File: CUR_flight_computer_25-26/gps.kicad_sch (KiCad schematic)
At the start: 4 parts, among them U1 SAM-M8Q

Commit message: Revert "edited gps"
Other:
- note removed: "Leave as 0 for now can be used for emi protection (R>20), ferrite beads, inductors but may affect signal timing"
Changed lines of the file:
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@@
 	(generator_version "9.0")
 	(paper "A4")
-	(text "Leave as 0 for now\ncan be used for emi protection\n(R>20), ferrite beads, inductors\nbut may affect signal timing"
-		(exclude_from_sim no)
-		(at 179.578 92.964 0)
-		(effects
-			(font
-				(size 1.27 1.27)
-			)
-		)
-	)
 	(text "Funky ass RX/TX switcher"
 		(exclude_from_sim no)

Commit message: added dubugging
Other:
- moved on the sheet: C13, R1, R2, U1

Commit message: hooked up more pins
added lcd header as well
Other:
- note added: "reset has internal pull up resistor"
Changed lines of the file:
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@@
+		)
+	)
+	(text "reset has internal pull up resistor\n"
+		(exclude_from_sim no)
+		(at 43.688 61.976 0)
+		(effects
+			(font
+				(size 1.27 1.27)
+			)
 		)
 	)
 	(text "connect safe boot to solderable pad"
 		(exclude_from_sim no)
-		(at 42.926 64.008 0)
+		(at 42.926 67.564 0)
 		(effects
 			(font
@@
 	(wire
 		(pts
-			(xy 58.42 58.42) (xy 62.23 58.42)
-		)
-		(stroke
-			(width 0)
-			(type default)
-		)
-	)
-	(wire
-		(pts
 			(xy 58.42 53.34) (xy 62.23 53.34)
 		)
@@
 		)
 		(stroke
+			(width 0)
+			(type default)
+		)
+	)
+	(wire
+		(pts
+			(xy 58.42 58.42) (xy 62.23 58.42)
+		)
+		(stroke

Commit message: updated all needed fixes
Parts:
- removed R1, R2: 0, symbol Device:R_Small
- added J7: Conn_01x02_Pin, symbol Connector:Conn_01x02_Pin
- added R28, R29: 0, symbol Device:R_Small_US
- renumbered C13 to C33, U1 to U11
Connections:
- net GPS_RX: now also R29.2
- net GPS_TX: now also R28.2
- net at U11.14 (RXD): now also R28.1
- net at U11.13 (TXD): now also R29.1
- net at U11.12 (SCL): now also J7.2 (Pin_2)
- net at U11.9 (SDA): now also J7.1 (Pin_1)
- no-connect marks 3 -> 1
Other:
- note added: "external reprogramming header"
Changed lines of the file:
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@@
 	(generator_version "9.0")
 	(paper "A4")
+	(text "external reprogramming header\n"
+		(exclude_from_sim no)
+		(at 105.41 62.23 0)
+		(effects
+			(font
+				(size 1.27 1.27)
+			)
+		)
+	)
 	(text "Funky ass RX/TX switcher"
 		(exclude_from_sim no)
-		(at 105.41 57.15 0)
+		(at 125.476 49.022 0)
 		(effects
 			(font
@@
 	)
 	(no_connect
-		(at 87.63 55.88)
-	)
-	(no_connect
 		(at 62.23 55.88)
 	)
-	(no_connect
-		(at 87.63 58.42)
-	)
 	(wire
 		(pts
@@
 	(wire
 		(pts
+			(xy 96.52 55.88) (xy 87.63 55.88)
+		)
+		(stroke
+			(width 0)
+			(type default)
+		)
+	)
+	(wire
+		(pts
 			(xy 57.15 36.83) (xy 57.15 39.37)
 		)
@@
 		(pts
 			(xy 87.63 50.8) (xy 90.17 50.8)
+		)
+		(stroke
+			(width 0)
+			(type default)
+		)
+	)
+	(wire
+		(pts
+			(xy 96.52 58.42) (xy 87.63 58.42)
 		)
 		(stroke
@@
 		(dnp no)
 		(fields_autoplaced yes)
-		(property "Reference" "#PWR012"
+		(property "Reference" "#PWR089"
 			(at 72.39 31.75 0)
 			(effects
@@
 			(project ""
 				(path "/bf7761cc-1b32-4d86-809c-5f027005229b/e838d24c-cb75-4a46-b88f-e4466a269629"
-					(reference "#PWR012")
+					(reference "#PWR089")
 					(unit 1)
 				)
@@
 		(dnp no)
 		(fields_autoplaced yes)
-		(property "Reference" "#PWR013"
+		(property "Reference" "#PWR088"
 			(at 57.15 45.72 0)
 			(effects
@@
 			(project ""
 				(path "/bf7761cc-1b32-4d86-809c-5f027005229b/e838d24c-cb75-4a46-b88f-e4466a269629"
-					(reference "#PWR013")
+					(reference "#PWR088")
 					(unit 1)
 				)
@@
 	)
 	(symbol
-		(lib_id "Device:R_Small")
-		(at 92.71 48.26 90)
+		(lib_id "Connector:Conn_01x02_Pin")
+		(at 101.6 55.88 0)
+		(mirror y)
 		(unit 1)
 		(exclude_from_sim no)
@@
 		(on_board yes)
 		(dnp no)
-		(property "Reference" "R1"
-			(at 92.71 43.942 90)
-			(effects
-				(font
-					(size 1.016 1.016)
-				)
-			)
-		)
-		(property "Value" "0"
-			(at 92.71 45.72 90)
-			(effects
-				(font
-					(size 1.27 1.27)
-				)
+		(fields_autoplaced yes)
+		(property "Reference" "J7"
+			(at 102.87 55.8799 0)
+			(effects
+				(font
+					(size 1.27 1.27)
+				)
+				(justify right)
+			)
+		)
+		(property "Value" "Conn_01x02_Pin"
+			(at 102.87 58.4199 0)
+			(effects
+				(font
+					(size 1.27 1.27)
+				)
+				(justify right)
 			)
 		)
 		(property "Footprint" ""
-			(at 92.71 48.26 0)
+			(at 101.6 55.88 0)
 			(effects
 				(font
@@
 		)
 		(property "Datasheet" "~"
-			(at 92.71 48.26 0)
-			(effects
-				(font
-					(size 1.27 1.27)
-				)
-				(hide yes)
-			)
-		)
-		(property "Description" "Resistor, small symbol"
-			(at 92.71 48.26 0)
+			(at 101.6 55.88 0)
+			(effects
+				(font
+					(size 1.27 1.27)
+				)
+				(hide yes)
+			)
+		)
+		(property "Description" "Generic connector, single row, 01x02, script generated"
+			(at 101.6 55.88 0)
 			(effects
 				(font
@@
 			(project ""
 				(path "/bf7761cc-1b32-4d86-809c-5f027005229b/e838d24c-cb75-4a46-b88f-e4466a269629"
-					(reference "R1")
+					(reference "J7")
 					(unit 1)
 				)
@@
 		(dnp no)
 		(fields_autoplaced yes)
-		(property "Reference" "#PWR014"
+		(property "Reference" "#PWR090"
 			(at 74.93 72.39 0)
 			(effects
@@
 			(project ""
 				(path "/bf7761cc-1b32-4d86-809c-5f027005229b/e838d24c-cb75-4a46-b88f-e4466a269629"
-					(reference "#PWR014")
+					(reference "#PWR090")
+					(unit 1)
+				)
+			)
+		)
+	)
+	(symbol
+		(lib_id "Device:R_Small_US")
+		(at 92.71 50.8 90)
+		(mirror x)
+		(unit 1)
+		(exclude_from_sim no)
+		(in_bom yes)
+		(on_board yes)
+		(dnp no)
+		(property "Reference" "R29"
+			(at 95.758 52.832 90)
+			(effects
+				(font
+					(size 1.27 1.27)
+				)
+			)
+		)
+		(property "Value" "0"
+			(at 92.71 52.832 90)
+			(effects
+				(font
+					(size 1.27 1.27)
+				)
+			)
+		)
+		(property "Footprint" ""
+			(at 92.71 50.8 0)
+			(effects
+				(font
+					(size 1.27 1.27)
+				)
+				(hide yes)
+			)
+		)
+		(property "Datasheet" "~"
+			(at 92.71 50.8 0)
+			(effects
+				(font
+					(size 1.27 1.27)
+				)
+				(hide yes)
+			)
+		)
+		(property "Description" "Resistor, small US symbol"
+			(at 92.71 50.8 0)
+			(effects
+				(font
+					(size 1.27 1.27)
+				)
+				(hide yes)
+			)
+		)
+		(pin "1"
+		)
+		(pin "2"
+		)
+		(instances
+			(project "CUR_flight_computer_25-26"
+				(path "/bf7761cc-1b32-4d86-809c-5f027005229b/e838d24c-cb75-4a46-b88f-e4466a269629"
+					(reference "R29")
+					(unit 1)
+				)
+			)
+		)
+	)
+	(symbol
+		(lib_id "Device:R_Small_US")
+		(at 92.71 48.26 90)
+		(unit 1)
+		(exclude_from_sim no)
+		(in_bom yes)
+		(on_board yes)
+		(dnp no)
+		(fields_autoplaced yes)
+		(property "Reference" "R28"
+			(at 92.71 41.91 90)
+			(effects
+				(font
+					(size 1.27 1.27)
+				)
+			)
+		)
+		(property "Value" "0"
+			(at 92.71 44.45 90)
+			(effects
+				(font
+					(size 1.27 1.27)
+				)
+			)
+		)
+		(property "Footprint" ""
+			(at 92.71 48.26 0)
+			(effects
+				(font
+					(size 1.27 1.27)
+				)
+				(hide yes)
+			)
+		)
+		(property "Datasheet" "~"
+			(at 92.71 48.26 0)
+			(effects
+				(font
+					(size 1.27 1.27)
+				)
+				(hide yes)
+			)
+		)
+		(property "Description" "Resistor, small US symbol"
+			(at 92.71 48.26 0)
+			(effects
+				(font
+					(size 1.27 1.27)
+				)
+				(hide yes)
+			)
+		)
+		(pin "1"
+		)
+		(pin "2"
+		)
+		(instances
+			(project ""
+				(path "/bf7761cc-1b32-4d86-809c-5f027005229b/e838d24c-cb75-4a46-b88f-e4466a269629"
+					(reference "R28")
 					(unit 1)
 				)
@@
 		(dnp no)
 		(fields_autoplaced yes)
-		(property "Reference" "C13"
+		(property "Reference" "C33"
 			(at 59.69 33.0262 0)
 			(effects
@@
 			(project ""
 				(path "/bf7761cc-1b32-4d86-809c-5f027005229b/e838d24c-cb75-4a46-b88f-e4466a269629"
-					(reference "C13")
-					(unit 1)
-				)
-			)
-		)
-	)
-	(symbol
-		(lib_id "Device:R_Small")
-		(at 92.71 50.8 90)
-		(unit 1)
-		(exclude_from_sim no)
-		(in_bom yes)
-		(on_board yes)
-		(dnp no)
-		(property "Reference" "R2"
-			(at 92.71 52.578 90)
-			(effects
-				(font
-					(size 1.016 1.016)
-				)
-			)
-		)
-		(property "Value" "0"
-			(at 92.71 54.102 90)
-			(effects
-				(font
-					(size 1.27 1.27)
-				)
-			)
-		)
-		(property "Footprint" ""
-			(at 92.71 50.8 0)
-			(effects
-				(font
-					(size 1.27 1.27)
-				)
-				(hide yes)
-			)
-		)
-		(property "Datasheet" "~"
-			(at 92.71 50.8 0)
-			(effects
-				(font
-					(size 1.27 1.27)
-				)
-				(hide yes)
-			)
-		)
-		(property "Description" "Resistor, small symbol"
-			(at 92.71 50.8 0)
-			(effects
-				(font
-					(size 1.27 1.27)
-				)
-				(hide yes)
-			)
-		)
-		(pin "2"
-		)
-		(pin "1"
-		)
-		(instances
-			(project ""
-				(path "/bf7761cc-1b32-4d86-809c-5f027005229b/e838d24c-cb75-4a46-b88f-e4466a269629"
-					(reference "R2")
+					(reference "C33")
 					(unit 1)
 				)
@@
 		(dnp no)
 		(fields_autoplaced yes)
-		(property "Reference" "U1"
+		(property "Reference" "U11"
 			(at 77.0733 66.04 0)
 			(effects
@@
 			(project ""
 				(path "/bf7761cc-1b32-4d86-809c-5f027005229b/e838d24c-cb75-4a46-b88f-e4466a269629"
-					(reference "U1")
+					(reference "U11")
 					(unit 1)
 				)

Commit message: assigned footrpint
need to double check:
- HSE
- Capacitors

for some unknown reason cur kicad library refuses to work
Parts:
- C33: footprint (none) -> Capacitor_SMD:C_0603_1608Metric
- J7: footprint (none) -> Connector_PinHeader_2.54mm:PinHeader_1x02_P2.54mm_Vertical
- R28, R29: footprint (none) -> Resistor_SMD:R_0603_1608Metric
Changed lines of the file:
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@@
 			)
 		)
-		(property "Footprint" ""
+		(property "Footprint" "Connector_PinHeader_2.54mm:PinHeader_1x02_P2.54mm_Vertical"
 			(at 101.6 55.88 0)
 			(effects
@@
 			)
 		)
-		(property "Footprint" ""
+		(property "Footprint" "Resistor_SMD:R_0603_1608Metric"
 			(at 92.71 50.8 0)
 			(effects
@@
 			)
 		)
-		(property "Footprint" ""
+		(property "Footprint" "Resistor_SMD:R_0603_1608Metric"
 			(at 92.71 48.26 0)
 			(effects
@@
 			)
 		)
-		(property "Footprint" ""
+		(property "Footprint" "Capacitor_SMD:C_0603_1608Metric"
 			(at 57.15 34.29 0)
 			(effects

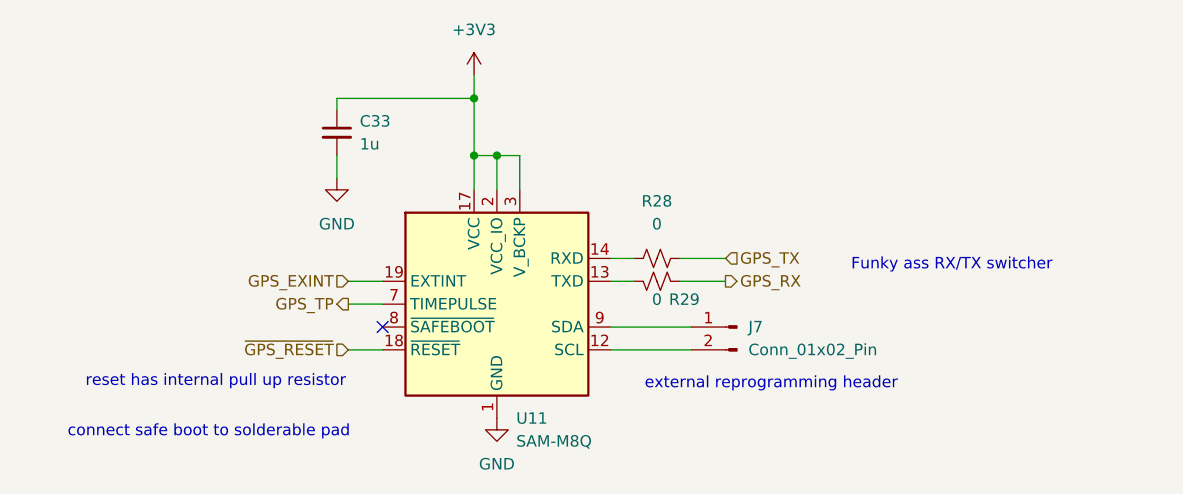
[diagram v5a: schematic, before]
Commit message: added testpoints to schematic
need to update layout
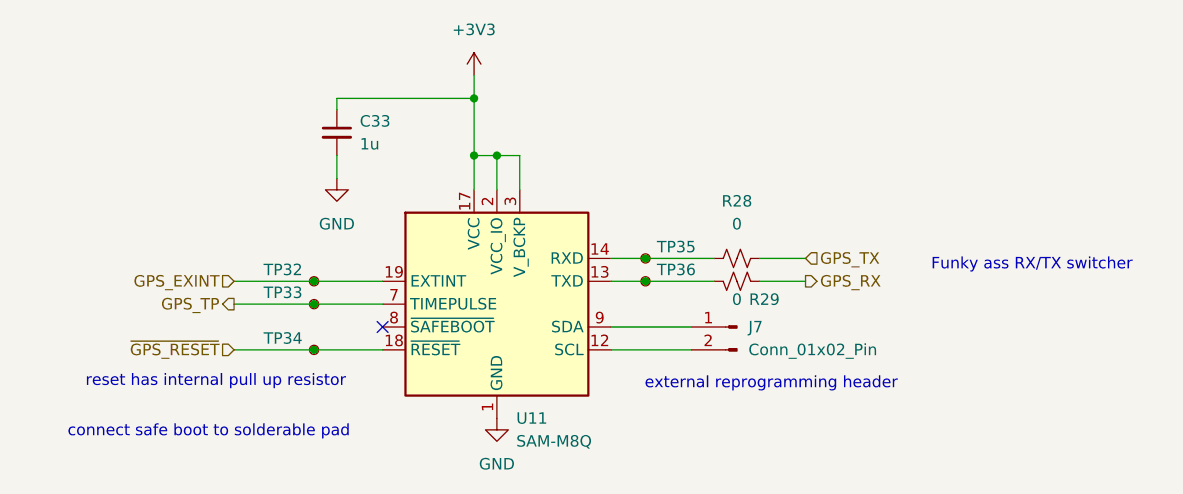
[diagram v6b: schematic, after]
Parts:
- added TP32, TP33, TP34, TP35, TP36: TestPoint_Small, TestPoint_KOASpeer:TestPoint_Chip_RCUCTE_0603, symbol Connector:TestPoint_Small
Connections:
- net GPS_EXINT: now also TP32.1
- net GPS_TP: now also TP33.1
- net ~{GPS_RESET}: now also TP34.1
- net at R29.1, U11.13 (TXD): now also TP36.1
- net at R28.1, U11.14 (RXD): now also TP35.1
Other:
- moved on the sheet: R28, R29

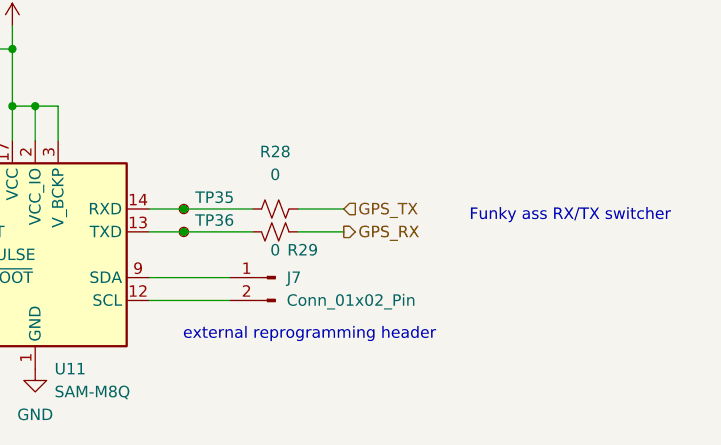
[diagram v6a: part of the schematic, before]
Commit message: Layout GPS and LoRa
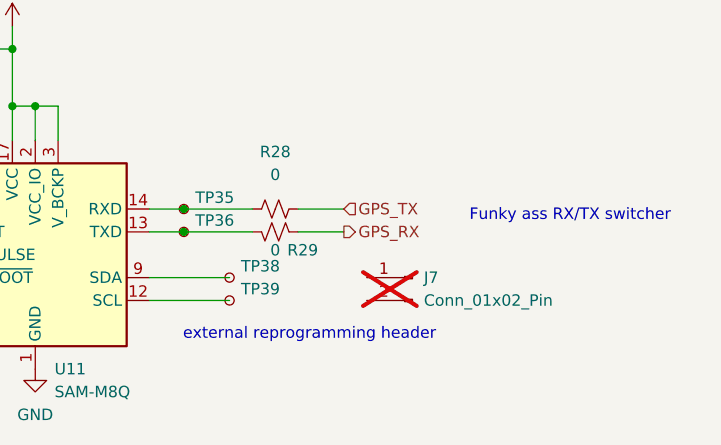
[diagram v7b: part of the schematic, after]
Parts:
- added TP38, TP39: TestPoint_Small, TestPoint_KOASpeer:TestPoint_Chip_RCUCTE_0603, symbol Connector:TestPoint_Small
- J7: now not fitted; now left out of the parts list
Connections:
- net at J7.1 (Pin_1): no longer U11.9 (SDA)
- net at J7.2 (Pin_2): no longer U11.12 (SCL)
- new net: TP39.1, U11.12 (SCL)
- new net: TP38.1, U11.9 (SDA)
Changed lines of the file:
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@@
 	(symbol
 		(lib_id "Connector:Conn_01x02_Pin")
-		(at 101.6 55.88 0)
+		(at 116.84 55.88 0)
 		(mirror y)
 		(unit 1)
 		(exclude_from_sim no)
-		(in_bom yes)
-		(on_board yes)
-		(dnp no)
+		(in_bom no)
+		(on_board no)
+		(dnp yes)
 		(fields_autoplaced yes)
 		(property "Reference" "J7"
-			(at 102.87 55.8799 0)
+			(at 118.11 55.8799 0)
 			(effects
 				(font
@@
 		)
 		(property "Value" "Conn_01x02_Pin"
-			(at 102.87 58.4199 0)
+			(at 118.11 58.4199 0)
 			(effects
 				(font
@@
 		)
 		(property "Footprint" "Connector_PinHeader_2.54mm:PinHeader_1x02_P2.54mm_Vertical"
-			(at 101.6 55.88 0)
-			(effects
-				(font
-					(size 1.27 1.27)
-				)
-				(hide yes)
-			)
-		)
-		(property "Datasheet" "~"
-			(at 101.6 55.88 0)
+			(at 116.84 55.88 0)
+			(effects
+				(font
+					(size 1.27 1.27)
+				)
+				(hide yes)
+			)
+		)
+		(property "Datasheet" "~"
+			(at 116.84 55.88 0)
 			(effects
 				(font
@@
 		)
 		(property "Description" "Generic connector, single row, 01x02, script generated"
-			(at 101.6 55.88 0)
+			(at 116.84 55.88 0)
 			(effects
 				(font
@@
 				(path "/bf7761cc-1b32-4d86-809c-5f027005229b/e838d24c-cb75-4a46-b88f-e4466a269629"
 					(reference "#PWR090")
+					(unit 1)
+				)
+			)
+		)
+	)
+	(symbol
+		(lib_id "Connector:TestPoint_Small")
+		(at 96.52 58.42 0)
+		(unit 1)
+		(exclude_from_sim no)
+		(in_bom yes)
+		(on_board yes)
+		(dnp no)
+		(fields_autoplaced yes)
+		(property "Reference" "TP39"
+			(at 97.79 57.1499 0)
+			(effects
+				(font
+					(size 1.27 1.27)
+				)
+				(justify left)
+			)
+		)
+		(property "Value" "TestPoint_Small"
+			(at 97.79 59.6899 0)
+			(effects
+				(font
+					(size 1.27 1.27)
+				)
+				(justify left)
+				(hide yes)
+			)
+		)
+		(property "Footprint" "TestPoint_KOASpeer:TestPoint_Chip_RCUCTE_0603"
+			(at 101.6 58.42 0)
+			(effects
+				(font
+					(size 1.27 1.27)
+				)
+				(hide yes)
+			)
+		)
+		(property "Datasheet" "~"
+			(at 101.6 58.42 0)
+			(effects
+				(font
+					(size 1.27 1.27)
+				)
+				(hide yes)
+			)
+		)
+		(property "Description" "test point"
+			(at 96.52 58.42 0)
+			(effects
+				(font
+					(size 1.27 1.27)
+				)
+				(hide yes)
+			)
+		)
+		(pin "1"
+		)
+		(instances
+			(project "CUR_flight_computer_25-26"
+				(path "/bf7761cc-1b32-4d86-809c-5f027005229b/e838d24c-cb75-4a46-b88f-e4466a269629"
+					(reference "TP39")
 					(unit 1)
 				)
@@
 					(unit 1)
 				)
+			)
+		)
+	)
+	(symbol
+		(lib_id "Connector:TestPoint_Small")
+		(at 96.52 55.88 0)
+		(unit 1)
+		(exclude_from_sim no)
+		(in_bom yes)
+		(on_board yes)
+		(dnp no)
+		(fields_autoplaced yes)
+		(property "Reference" "TP38"
+			(at 97.79 54.6099 0)
+			(effects
+				(font
+					(size 1.27 1.27)
+				)
+				(justify left)
+			)
+		)
+		(property "Value" "TestPoint_Small"
+			(at 97.79 57.1499 0)
+			(effects
+				(font
+					(size 1.27 1.27)
+				)
+				(justify left)
+				(hide yes)
+			)
+		)
+		(property "Footprint" "TestPoint_KOASpeer:TestPoint_Chip_RCUCTE_0603"
+			(at 101.6 55.88 0)
+			(effects
+				(font
+					(size 1.27 1.27)
+				)
+				(hide yes)
+			)
+		)
+		(property "Datasheet" "~"
+			(at 101.6 55.88 0)
+			(effects
+				(font
+					(size 1.27 1.27)
+				)
+				(hide yes)
+			)
+		)
+		(property "Description" "test point"
+			(at 96.52 55.88 0)
+			(effects
+				(font
+					(size 1.27 1.27)
+				)
+				(hide yes)
+			)
+		)
+		(pin "1"
+		)
+		(instances
+			(project "CUR_flight_computer_25-26"
+				(path "/bf7761cc-1b32-4d86-809c-5f027005229b/e838d24c-cb75-4a46-b88f-e4466a269629"
+					(reference "TP38")
+					(unit 1)
+				)

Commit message: Delete reprogramming header
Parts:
- removed J7: Conn_01x02_Pin, Connector_PinHeader_2.54mm:PinHeader_1x02_P2.54mm_Vertical, symbol Connector:Conn_01x02_Pin
- C33: MPN (none) -> C0603C105K4RACTU
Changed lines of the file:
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@@
-	)
-	(symbol
-		(lib_id "Connector:Conn_01x02_Pin")
-		(at 116.84 55.88 0)
-		(mirror y)
-		(unit 1)
-		(exclude_from_sim no)
-		(in_bom no)
-		(on_board no)
-		(dnp yes)
-		(fields_autoplaced yes)
-		(property "Reference" "J7"
-			(at 118.11 55.8799 0)
-			(effects
-				(font
-					(size 1.27 1.27)
-				)
-				(justify right)
-			)
-		)
-		(property "Value" "Conn_01x02_Pin"
-			(at 118.11 58.4199 0)
-			(effects
-				(font
-					(size 1.27 1.27)
-				)
-				(justify right)
-			)
-		)
-		(property "Footprint" "Connector_PinHeader_2.54mm:PinHeader_1x02_P2.54mm_Vertical"
-			(at 116.84 55.88 0)
-			(effects
-				(font
-					(size 1.27 1.27)
-				)
-				(hide yes)
-			)
-		)
-		(property "Datasheet" "~"
-			(at 116.84 55.88 0)
-			(effects
-				(font
-					(size 1.27 1.27)
-				)
-				(hide yes)
-			)
-		)
-		(property "Description" "Generic connector, single row, 01x02, script generated"
-			(at 116.84 55.88 0)
-			(effects
-				(font
-					(size 1.27 1.27)
-				)
-				(hide yes)
-			)
-		)
-		(pin "1"
-		)
-		(pin "2"
-		)
-		(instances
-			(project ""
-				(path "/bf7761cc-1b32-4d86-809c-5f027005229b/e838d24c-cb75-4a46-b88f-e4466a269629"
-					(reference "J7")
-					(unit 1)
-				)
-			)
-		)
 	)
 	(symbol
@@
 			)
 		)
+		(property "MPN" "C0603C105K4RACTU"
+			(at 57.15 34.29 0)
+			(effects
+				(font
+					(size 1.27 1.27)
+				)
+			)
+		)
